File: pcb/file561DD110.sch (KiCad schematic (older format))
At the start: 32 parts, among them P12 CONN_01X02, P16 FAN, Q18 BC849, Q19 IRF9530, Q20 BC849, Q21 CSD18536KCS, Q22 IRFR3607PBF, Q23 BC849, Q24 BC849, U6 LM358DUAL

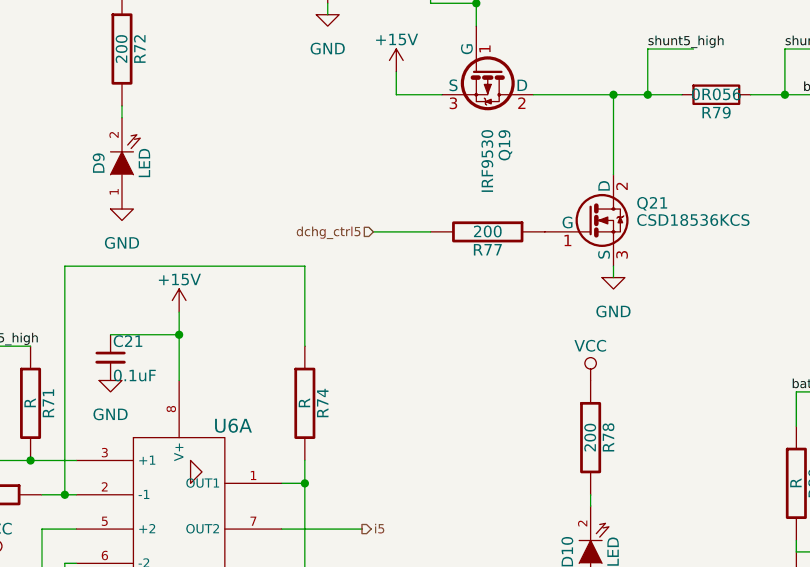
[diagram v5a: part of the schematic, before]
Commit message: Added caps on discharge fet gates
Need to filter the digital signal from the MCU to create an analog
voltage at the gate because the fet should operate in between on and
off states (which generates heat due to high Rds).
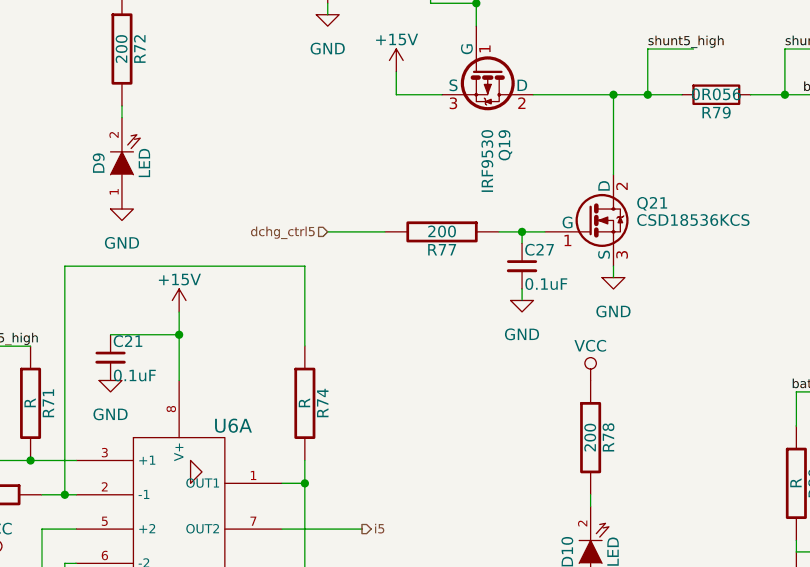
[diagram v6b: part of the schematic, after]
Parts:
- added C27: 0.1uF, Capacitors_SMD:C_0805_HandSoldering, symbol C_Small
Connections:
- net GND: now also C27.2
- net at Q21.1 (G), R77.1: now also C27.1
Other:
- moved on the sheet: R77
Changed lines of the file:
@@
 $EndComp
 $Comp
-L +15V #PWR086
+L +15V #PWR112
 U 1 1 561DD756
 P 3750 800
-F 0 "#PWR086" H 3750 650 50  0001 C CNN
+F 0 "#PWR112" H 3750 650 50  0001 C CNN
 F 1 "+15V" H 3750 940 50  0000 C CNN
 F 2 "" H 3750 800 60  0000 C CNN
@@
 $EndComp
 $Comp
-L GND-RESCUE-BatAger #PWR087
+L GND-RESCUE-BatAger #PWR110
 U 1 1 561DD75C
 P 3100 1450
-F 0 "#PWR087" H 3100 1200 50  0001 C CNN
+F 0 "#PWR110" H 3100 1200 50  0001 C CNN
 F 1 "GND" H 3100 1300 50  0000 C CNN
 F 2 "" H 3100 1450 60  0000 C CNN
@@
 $EndComp
 $Comp
-L GND-RESCUE-BatAger #PWR088
+L GND-RESCUE-BatAger #PWR116
 U 1 1 561DD769
 P 4350 2600
-F 0 "#PWR088" H 4350 2350 50  0001 C CNN
+F 0 "#PWR116" H 4350 2350 50  0001 C CNN
 F 1 "GND" H 4350 2450 50  0000 C CNN
 F 2 "" H 4350 2600 60  0000 C CNN
@@
 L R-RESCUE-BatAger R77
 U 1 1 561DD776
-P 3800 2400
-F 0 "R77" V 3880 2400 50  0000 C CNN
-F 1 "200" V 3800 2400 50  0000 C CNN
-F 2 "Resistors_SMD:R_0805_HandSoldering" V 3730 2400 30  0001 C CNN
-F 3 "" H 3800 2400 30  0000 C CNN
-	1    3800 2400
+P 3600 2400
+F 0 "R77" V 3680 2400 50  0000 C CNN
+F 1 "200" V 3600 2400 50  0000 C CNN
+F 2 "Resistors_SMD:R_0805_HandSoldering" V 3530 2400 30  0001 C CNN
+F 3 "" H 3600 2400 30  0000 C CNN
+	1    3600 2400
 	0    1    1    0
 $EndComp
 $Comp
-L GND-RESCUE-BatAger #PWR089
+L GND-RESCUE-BatAger #PWR115
 U 1 1 561DD77D
 P 4250 4550
-F 0 "#PWR089" H 4250 4300 50  0001 C CNN
+F 0 "#PWR115" H 4250 4300 50  0001 C CNN
 F 1 "GND" H 4250 4400 50  0000 C CNN
 F 2 "" H 4250 4550 60  0000 C CNN
@@
 $EndComp
 $Comp
-L GND-RESCUE-BatAger #PWR090
+L GND-RESCUE-BatAger #PWR106
 U 1 1 561DD783
 P 2200 2300
-F 0 "#PWR090" H 2200 2050 50  0001 C CNN
+F 0 "#PWR106" H 2200 2050 50  0001 C CNN
 F 1 "GND" H 2200 2150 50  0000 C CNN
 F 2 "" H 2200 2300 60  0000 C CNN
@@
 $EndComp
 $Comp
-L +15V #PWR091
+L +15V #PWR107
 U 1 1 561DD797
 P 2450 2750
-F 0 "#PWR091" H 2450 2600 50  0001 C CNN
+F 0 "#PWR107" H 2450 2600 50  0001 C CNN
 F 1 "+15V" H 2450 2890 50  0000 C CNN
 F 2 "" H 2450 2750 60  0000 C CNN
@@
 $EndComp
 $Comp
-L -15V #PWR104
+L -15V #PWR108
 U 1 1 561DD79D
 P 2450 4400
-F 0 "#PWR104" H 2450 4250 50  0001 C CNN
+F 0 "#PWR108" H 2450 4250 50  0001 C CNN
 F 1 "-15V" H 2450 4540 50  0000 C CNN
 F 2 "" H 2450 4400 60  0000 C CNN
@@
 $EndComp
 $Comp
-L GND-RESCUE-BatAger #PWR092
+L GND-RESCUE-BatAger #PWR97
 U 1 1 561DD7B1
 P 1150 4100
-F 0 "#PWR092" H 1150 3850 50  0001 C CNN
+F 0 "#PWR97" H 1150 3850 50  0001 C CNN
 F 1 "GND" H 1150 3950 50  0000 C CNN
 F 2 "" H 1150 4100 60  0000 C CNN
@@
 $EndComp
 $Comp
-L GND-RESCUE-BatAger #PWR093
+L GND-RESCUE-BatAger #PWR103
 U 1 1 561DD7D5
 P 1650 4900
-F 0 "#PWR093" H 1650 4650 50  0001 C CNN
+F 0 "#PWR103" H 1650 4650 50  0001 C CNN
 F 1 "GND" H 1650 4750 50  0000 C CNN
 F 2 "" H 1650 4900 60  0000 C CNN
@@
 $EndComp
 $Comp
-L VCC #PWR094
+L VCC #PWR102
 U 1 1 561DD7DB
 P 1650 3850
-F 0 "#PWR094" H 1650 3700 50  0001 C CNN
+F 0 "#PWR102" H 1650 3700 50  0001 C CNN
 F 1 "VCC" H 1650 4000 50  0000 C CNN
 F 2 "" H 1650 3850 60  0000 C CNN
@@
 	1950 1200 2300 1200
 $Comp
-L +15V #PWR095
+L +15V #PWR111
 U 1 1 561DD811
 P 3400 1700
-F 0 "#PWR095" H 3400 1550 50  0001 C CNN
+F 0 "#PWR111" H 3400 1550 50  0001 C CNN
 F 1 "+15V" H 3400 1840 50  0000 C CNN
 F 2 "" H 3400 1700 60  0000 C CNN
@@
 Connection ~ 2200 1200
 Wire Wire Line
-	3550 2400 3300 2400
+	3350 2400 3100 2400
 Wire Wire Line
 	5150 3800 5150 3750
 $Comp
-L GND-RESCUE-BatAger #PWR096
+L GND-RESCUE-BatAger #PWR117
 U 1 1 561DD81F
 P 5150 4350
-F 0 "#PWR096" H 5150 4100 50  0001 C CNN
+F 0 "#PWR117" H 5150 4100 50  0001 C CNN
 F 1 "GND" H 5150 4200 50  0000 C CNN
 F 2 "" H 5150 4350 60  0000 C CNN
@@
 	3400 4250 3200 4250
 $Comp
-L VCC #PWR097
+L VCC #PWR114
 U 1 1 561DD82D
 P 4250 3050
-F 0 "#PWR097" H 4250 2900 50  0001 C CNN
+F 0 "#PWR114" H 4250 2900 50  0001 C CNN
 F 1 "VCC" H 4250 3200 50  0000 C CNN
 F 2 "" H 4250 3050 60  0000 C CNN
@@
 Text HLabel 1950 1200 0    40   Input ~ 0
 chg_ctrl5
-Text HLabel 3300 2400 0    40   Input ~ 0
+Text HLabel 3100 2400 0    40   Input ~ 0
 dchg_ctrl5
 Text HLabel 3250 3700 2    40   Output ~ 0
@@
 +15V
 $Comp
-L +15V #PWR098
+L +15V #PWR98
 U 1 1 561DE12A
 P 1200 5550
-F 0 "#PWR098" H 1200 5400 50  0001 C CNN
+F 0 "#PWR98" H 1200 5400 50  0001 C CNN
 F 1 "+15V" H 1200 5690 50  0000 C CNN
 F 2 "" H 1200 5550 60  0000 C CNN
@@
 GND
 $Comp
-L GND-RESCUE-BatAger #PWR099
+L GND-RESCUE-BatAger #PWR99
 U 1 1 561DE23B
 P 1200 5800
-F 0 "#PWR099" H 1200 5550 50  0001 C CNN
+F 0 "#PWR99" H 1200 5550 50  0001 C CNN
 F 1 "GND" H 1200 5650 50  0000 C CNN
 F 2 "" H 1200 5800 60  0000 C CNN
@@
 -15V
 $Comp
-L -15V #PWR97
+L -15V #PWR101
 U 1 1 561DE3BD
 P 1400 6050
-F 0 "#PWR97" H 1400 5900 50  0001 C CNN
+F 0 "#PWR101" H 1400 5900 50  0001 C CNN
 F 1 "-15V" H 1400 6190 50  0000 C CNN
 F 2 "" H 1400 6050 60  0000 C CNN
@@
 VCC
 $Comp
-L VCC #PWR0100
+L VCC #PWR100
 U 1 1 561DE52B
 P 1200 6350
-F 0 "#PWR0100" H 1200 6200 50  0001 C CNN
+F 0 "#PWR100" H 1200 6200 50  0001 C CNN
 F 1 "VCC" H 1200 6500 50  0000 C CNN
 F 2 "" H 1200 6350 60  0000 C CNN
@@
 $EndComp
 $Comp
-L GND-RESCUE-BatAger #PWR0101
+L GND-RESCUE-BatAger #PWR105
 U 1 1 561E5449
 P 2150 4650
-F 0 "#PWR0101" H 2150 4400 50  0001 C CNN
+F 0 "#PWR105" H 2150 4400 50  0001 C CNN
 F 1 "GND" H 2150 4500 50  0000 C CNN
 F 2 "" H 2150 4650 60  0000 C CNN
@@
 $EndComp
 $Comp
-L GND-RESCUE-BatAger #PWR0102
+L GND-RESCUE-BatAger #PWR104
 U 1 1 561E54E0
 P 2150 3050
-F 0 "#PWR0102" H 2150 2800 50  0001 C CNN
+F 0 "#PWR104" H 2150 2800 50  0001 C CNN
 F 1 "GND" H 2150 2900 50  0000 C CNN
 F 2 "" H 2150 3050 60  0000 C CNN
@@
 	3050 5750 2700 5750
 $Comp
-L GND-RESCUE-BatAger #PWR0103
+L GND-RESCUE-BatAger #PWR109
 U 1 1 561E5AC5
 P 2950 5950
-F 0 "#PWR0103" H 2950 5700 50  0001 C CNN
+F 0 "#PWR109" H 2950 5700 50  0001 C CNN
 F 1 "GND" H 2950 5800 50  0000 C CNN
 F 2 "" H 2950 5950 60  0000 C CNN
@@
 	8950 3000 8950 3100
 $Comp
-L GND #PWR0104
+L GND #PWR120
 U 1 1 561F6DC6
 P 8950 3600
-F 0 "#PWR0104" H 8950 3350 50  0001 C CNN
+F 0 "#PWR120" H 8950 3350 50  0001 C CNN
 F 1 "GND" H 8950 3450 50  0000 C CNN
 F 2 "" H 8950 3600 60  0000 C CNN
@@
 $EndComp
 $Comp
-L GND #PWR0105
+L GND #PWR119
 U 1 1 562109D3
 P 8500 3750
-F 0 "#PWR0105" H 8500 3500 50  0001 C CNN
+F 0 "#PWR119" H 8500 3500 50  0001 C CNN
 F 1 "GND" H 8500 3600 50  0000 C CNN
 F 2 "" H 8500 3750 60  0000 C CNN
@@
 $EndComp
 $Comp
-L GND #PWR0106
+L GND #PWR118
 U 1 1 56210A3E
 P 8050 3950
-F 0 "#PWR0106" H 8050 3700 50  0001 C CNN
+F 0 "#PWR118" H 8050 3700 50  0001 C CNN
 F 1 "GND" H 8050 3800 50  0000 C CNN
 F 2 "" H 8050 3950 60  0000 C CNN
@@
 Wire Wire Line
 	8500 3750 8500 3700
+$Comp
+L C_Small C27
+U 1 1 56267435
+P 3950 2550
+F 0 "C27" H 3960 2620 50  0000 L CNN
+F 1 "0.1uF" H 3960 2470 50  0000 L CNN
+F 2 "Capacitors_SMD:C_0805_HandSoldering" H 3950 2550 60  0001 C CNN
+F 3 "" H 3950 2550 60  0000 C CNN
+	1    3950 2550
+	1    0    0    -1
+$EndComp
+Wire Wire Line
+	3850 2400 4050 2400
+Wire Wire Line
+	3950 2450 3950 2400
+Connection ~ 3950 2400
+$Comp
+L GND-RESCUE-BatAger #PWR113
+U 1 1 562675C2
+P 3950 2700
+F 0 "#PWR113" H 3950 2450 50  0001 C CNN
+F 1 "GND" H 3950 2550 50  0000 C CNN
+F 2 "" H 3950 2700 60  0000 C CNN
+F 3 "" H 3950 2700 60  0000 C CNN
+	1    3950 2700
+	1    0    0    -1
+$EndComp
+Wire Wire Line
+	3950 2700 3950 2650
 $EndSCHEMATC

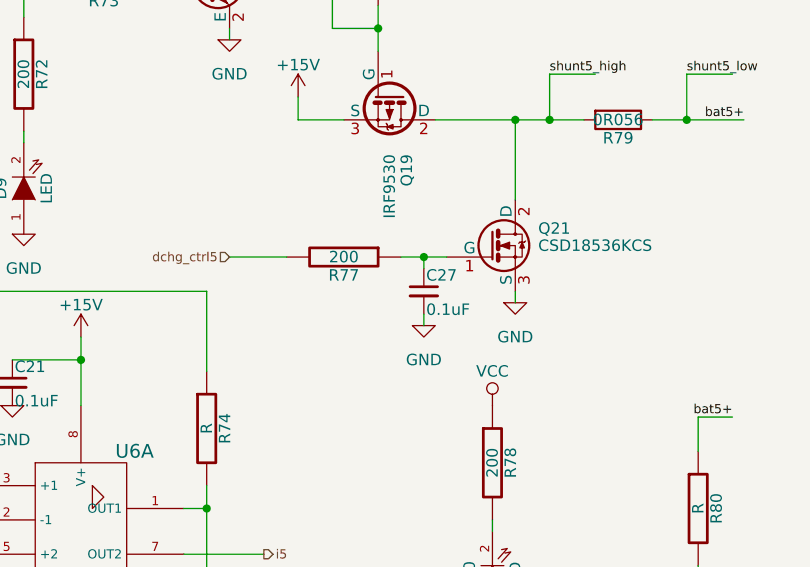
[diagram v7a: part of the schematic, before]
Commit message: Minor package changes.
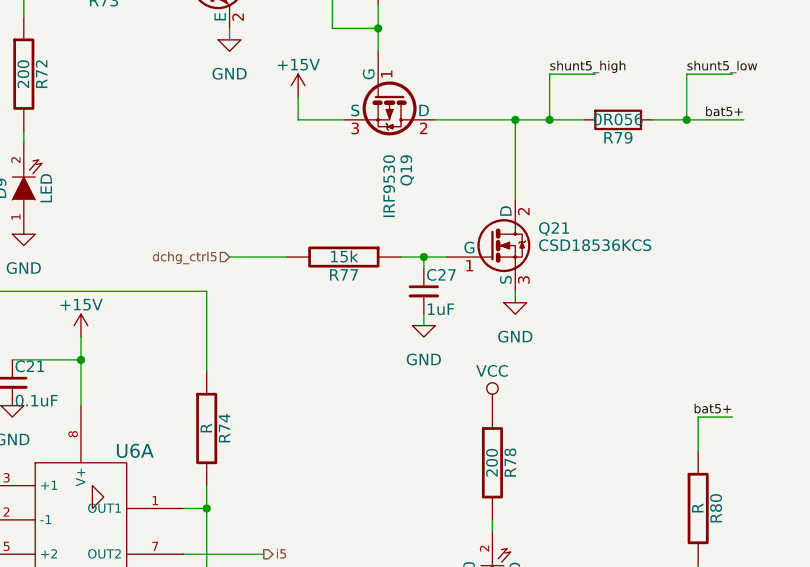
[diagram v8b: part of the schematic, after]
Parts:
- C27: value 0.1uF -> 1uF
- P12: footprint Pin_Headers:Pin_Header_Straight_1x02 -> Custom Footprints:PINHEAD1-2_200mil
- R77: value 200 -> 15k
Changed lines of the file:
@@
 P 3600 2400
 F 0 "R77" V 3680 2400 50  0000 C CNN
-F 1 "200" V 3600 2400 50  0000 C CNN
+F 1 "15k" V 3600 2400 50  0000 C CNN
 F 2 "Resistors_SMD:R_0805_HandSoldering" V 3530 2400 30  0001 C CNN
 F 3 "" H 3600 2400 30  0000 C CNN
@@
 F 0 "P12" H 3250 5950 50  0000 C CNN
 F 1 "CONN_01X02" V 3350 5800 50  0000 C CNN
-F 2 "Pin_Headers:Pin_Header_Straight_1x02" H 3250 5800 60  0001 C CNN
+F 2 "Custom Footprints:PINHEAD1-2_200mil" H 3250 5800 60  0001 C CNN
 F 3 "" H 3250 5800 60  0000 C CNN
 	1    3250 5800
@@
 P 3950 2550
 F 0 "C27" H 3960 2620 50  0000 L CNN
-F 1 "0.1uF" H 3960 2470 50  0000 L CNN
+F 1 "1uF" H 3960 2470 50  0000 L CNN
 F 2 "Capacitors_SMD:C_0805_HandSoldering" H 3950 2550 60  0001 C CNN
 F 3 "" H 3950 2550 60  0000 C CNN
